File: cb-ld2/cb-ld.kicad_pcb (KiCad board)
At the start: 4 copper layers, 25.4 x 55.8 mm, 24 parts, among them P1 CONN_01X14, P2 CONN_01X14, U1 SKY13385, U2 MGA-81563, U3 MBC13916, U4 SKY13385

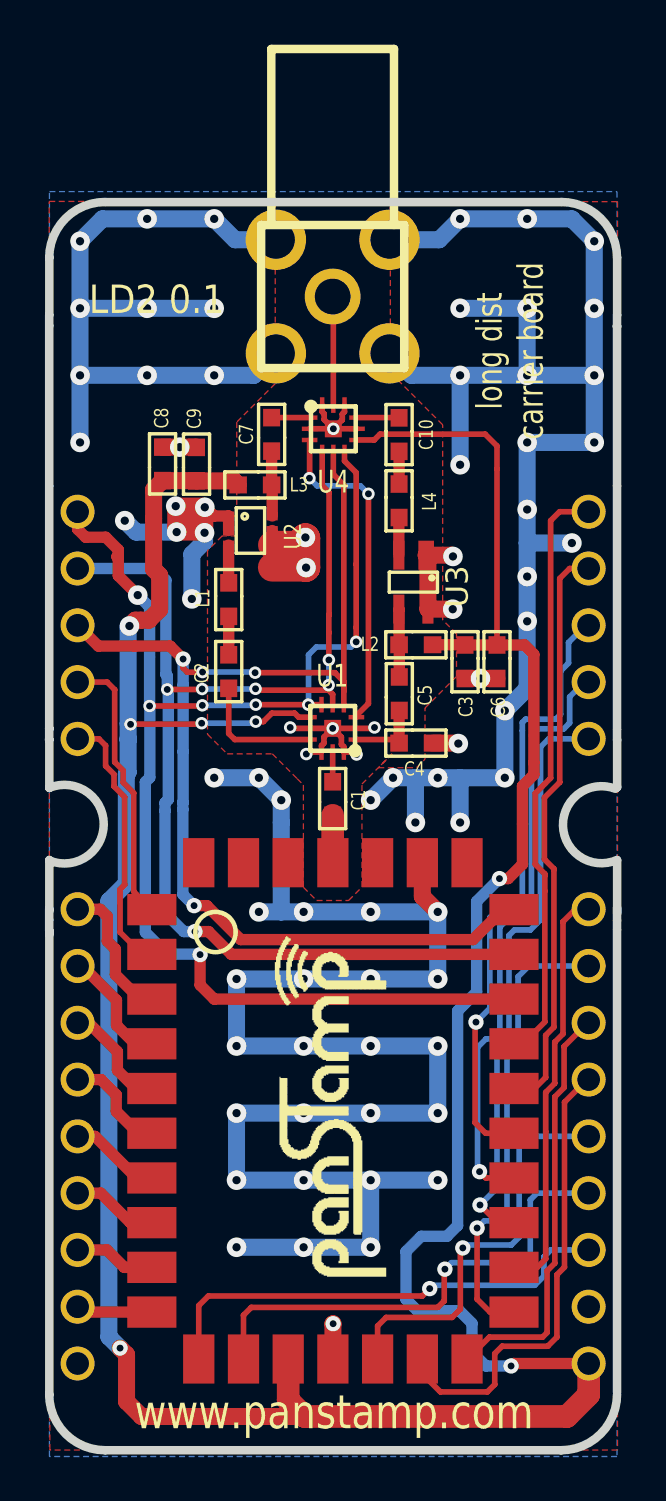
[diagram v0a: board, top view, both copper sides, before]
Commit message: Natural evolution of the design after doing some tests
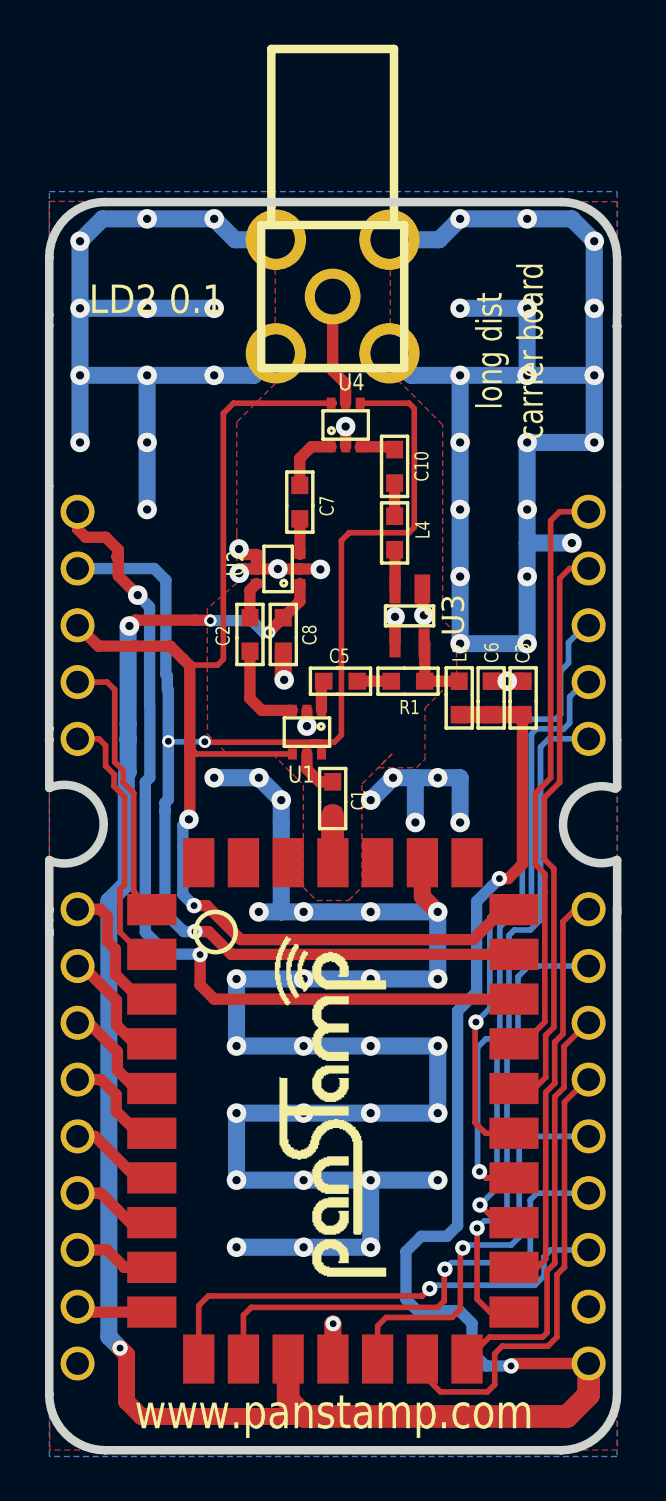
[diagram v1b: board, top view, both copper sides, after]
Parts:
- removed C4: 3p, mysmd:SM0603S
- removed C9: 100p, mysmd:SM0603S
- removed L1, L3: 10n, mysmd:SM0603S
- added R1: 24, mysmd:SM0603S, F.Cu at (200.7, 66.7)
- C2, C7: value 220p -> 100p
- C3: value 10n -> 100n
- C5: value 1.5p -> 2.4p
- C8: value 10n -> 470p
- L2: value 10n -> 33n
- L4: value 6.8n -> 39n
- U1, U4: value SKY13385 -> AS213-92; footprint mysmd:QFN12 -> mysmd:SC-70
- U2: value MGA-81563 -> BGA2817
- U3: footprint mysmd:SOT-343R -> SOT-343R
- moved C8 9.35 mm to (195.1, 64.6)
- moved C7 3.28 mm to (195.8, 58.7)
- moved L2 3.07 mm to (203.0, 67.4), turned to 90 degrees
- moved C3 3.06 mm to (205.8, 67.4), turned to 270 degrees
- moved C5 2.69 mm to (197.7, 66.7), turned to 180 degrees
- moved U2 2.12 mm to (194.9, 61.7), turned to 90 degrees
- moved C2 1.91 mm to (193.6, 64.6)
- moved C6 1.64 mm to (204.4, 67.4), turned to 270 degrees
- moved U3 1.52 mm to (200.7, 63.8)
- moved L4 1.45 mm to (200.1, 60.0)
- moved C10 1.43 mm to (200.1, 57.1)
- moved U1 1.16 mm to (196.2, 69.0)
- moved U4 0.58 mm to (197.9, 55.2)
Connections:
- C8 pad 1: GND -> VCC
- C8 pad 2: VCC -> GND
- L2 pad 2: Net-(C5-Pad1) -> Net-(L2-Pad2)
- P1 pad 1: /BYPASS -> /D20
- PS1 pad 25: /BYPASS -> /D20
- U1 pad 3: Net-(U1-Pad3) -> Net-(C2-Pad2)
- U1 pad 5: /D19 -> Net-(C1-Pad1)
- U1 pad 6: /BYPASS -> /D19
- U2 pad 1: GND -> VCC
- U2 pad 3: Net-(L1-Pad2) -> Net-(C7-Pad2)
- U2 pad 6: Net-(C7-Pad2) -> Net-(C2-Pad1)
- U3 pad 3: Net-(C5-Pad1) -> Net-(L2-Pad2)
- U4 pad 3: Net-(U1-Pad3) -> Net-(C10-Pad2)
- U4 pad 5: /D18 -> Net-(ANT1-Pad1)
- U4 pad 6: /BYPASS -> /D18
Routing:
- net /BYPASS: track 60.4 -> 0.00 mm, vias 7 -> 0
- net /D20: track 0.00 -> 39.4 mm, vias 0 -> 2
- net GND: track 223.6 -> 192.8 mm, vias 79 -> 68
- net VCC: track 143.2 -> 112.7 mm, vias 7 -> 6
- net Net-(U1-Pad3): track 14.9 -> 0.00 mm, vias 2 -> 0
- net /D19: track 55.4 -> 66.9 mm, vias 6 -> 3
- net (no net): track 0.00 -> 8.41 mm, vias 0 -> 5
- net Net-(L2-Pad2): track 0.00 -> 3.27 mm
- net /D18: track 51.8 -> 55.0 mm, vias 4 -> 2
- net Net-(C5-Pad2): track 3.44 -> 1.35 mm
- net Net-(L1-Pad2): track 1.69 -> 0.00 mm
- net Net-(C5-Pad1): track 3.04 -> 1.52 mm
- net Net-(C2-Pad2): track 5.72 -> 4.24 mm
- net Net-(C7-Pad2): track 2.91 -> 1.59 mm
- net Net-(C7-Pad1): track 1.70 -> 2.82 mm
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
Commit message: PA replaced by MGA82563
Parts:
- added L1: 22n, mysmd:SM0603S, F.Cu at (194.9, 59.3)
- added fiducial: VAL**, mymods:fiducial, F.Cu at (207.6, 47.6)
- added fiducial: VAL**, mymods:fiducial, F.Cu at (186.6, 99.6)
- C8: value 470p -> 100p
- U2: value BGA2817 -> MGA82563
- moved C8 6.79 mm to (194.9, 57.8), turned to 0 degrees
- moved C7 1.37 mm to (197.2, 58.6)
- moved U2 0.17 mm to (194.8, 61.5), turned to 270 degrees
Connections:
- U2 pad 1: VCC -> GND
- U2 pad 3: Net-(C7-Pad2) -> Net-(C2-Pad1)
- U2 pad 6: Net-(C2-Pad1) -> Net-(C7-Pad2)
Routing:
- net VCC: track 112.7 -> 115.1 mm
- net GND: track 192.8 -> 194.8 mm, vias 68 -> 69
- net Net-(C7-Pad2): track 1.59 -> 3.17 mm
- net Net-(C7-Pad1): track 2.82 -> 1.67 mm
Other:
- board text added: "LD2 0.2"
- board text removed: "LD2 0.1"

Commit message: Preparing board for 900 MHz
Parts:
- added C4: 3p, mysmd:SM0603S, F.Cu at (196.9, 64.5)
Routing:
- net Net-(C4-Pad2): track 1.35 -> 2.80 mm
- net GND: track 194.8 -> 195.7 mm
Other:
- board text added: "LD2 1.0"
- board text removed: "LD2 0.2"
